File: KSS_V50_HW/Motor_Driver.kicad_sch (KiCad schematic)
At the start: 19 parts, among them J3 Conn_01x04_Socket, U6 TMAG5328, U7 TMC2300-LA-T

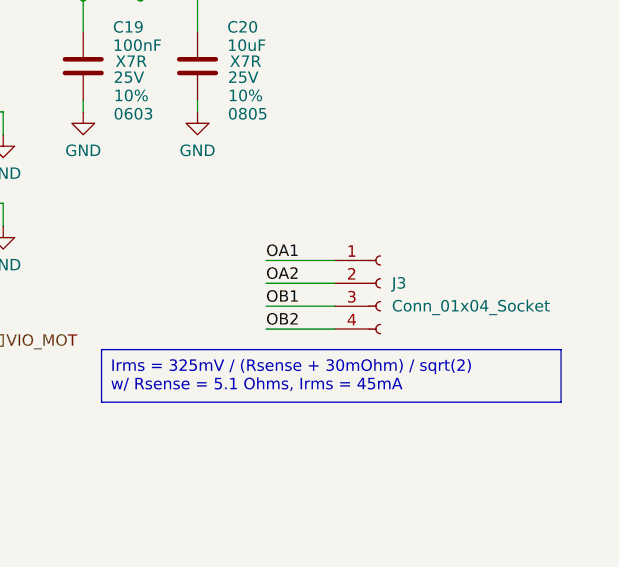
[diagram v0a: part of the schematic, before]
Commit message: minor changed based on Wilson's first review and personal layout round
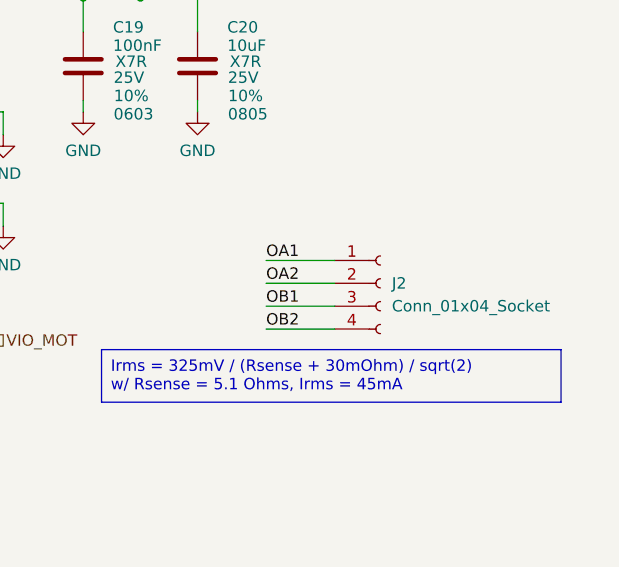
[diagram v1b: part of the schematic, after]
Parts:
- renumbered J3 to J2
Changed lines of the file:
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@@
 		(dnp no)
 		(fields_autoplaced yes)
-		(property "Reference" "J3"
+		(property "Reference" "J2"
 			(at 246.38 104.1399 0)
 			(effects

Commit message: Added fab outputs
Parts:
- U7: DPN (none) -> 175-TMC2300-LA-TCT-ND
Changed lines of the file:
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@@
+			)
+		)
+		(property "DPN" "175-TMC2300-LA-TCT-ND"
+			(at 157.48 95.25 0)
+			(effects
+				(font
+					(size 1.27 1.27)
+				)
+				(hide yes)
 			)
 		)
